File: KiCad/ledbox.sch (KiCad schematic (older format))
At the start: 0 parts

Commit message: Schematic Version 4 Some Software Changes
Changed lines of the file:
@@
 EESchema Schematic File Version 3
+LIBS:ledbox-rescue
 LIBS:power
 LIBS:device
@@
 LIBS:contrib
 LIBS:ledbox-newsymbols
+LIBS:74xxLVCxG
+LIBS:analog_devices
+LIBS:boards
+LIBS:bridge_rectifier
+LIBS:caf
+LIBS:cirrus logic
+LIBS:eeprom
+LIBS:ft232rl
+LIBS:linear_technology
+LIBS:micrel
+LIBS:NXP Semiconductor
+LIBS:SigmaDSP
+LIBS:texas_instruments
+LIBS:tl431
+LIBS:toslink
+LIBS:worldsemi
+LIBS:ac-dc
+LIBS:Altera
+LIBS:Battery_Management
+LIBS:bbd
+LIBS:Bosch
+LIBS:brooktre
+LIBS:Connector
+LIBS:dc-dc
+LIBS:Decawave
+LIBS:Diode
+LIBS:Display
+LIBS:driver_gate
+LIBS:DSP_Microchip_DSPIC33
+LIBS:elec-unifil
+LIBS:ESD_Protection
+LIBS:Espressif
+LIBS:FPGA_Actel
+LIBS:ftdi
+LIBS:gennum
+LIBS:Graphic
+LIBS:hc11
+LIBS:infineon
+LIBS:intersil
+LIBS:ir
+LIBS:Lattice
+LIBS:LED
+LIBS:LEM
+LIBS:Logic_74xgxx
+LIBS:Logic_74xx
+LIBS:Logic_CMOS_4000
+LIBS:Logic_CMOS_IEEE
+LIBS:logic_programmable
+LIBS:Logic_TTL_IEEE
+LIBS:maxim
+LIBS:MCU_Microchip_PIC10
+LIBS:MCU_Microchip_PIC12
+LIBS:MCU_Microchip_PIC16
+LIBS:MCU_Microchip_PIC18
+LIBS:MCU_Microchip_PIC24
+LIBS:MCU_Microchip_PIC32
+LIBS:MCU_NXP_Kinetis
+LIBS:MCU_NXP_LPC
+LIBS:MCU_NXP_S08
+LIBS:MCU_Parallax
+LIBS:MCU_ST_STM8
+LIBS:MCU_ST_STM32
+LIBS:MCU_Texas_MSP430
+LIBS:Mechanical
+LIBS:modules
+LIBS:motor_drivers
+LIBS:Motor
+LIBS:nordicsemi
+LIBS:nxp
+LIBS:onsemi
+LIBS:Oscillators
+LIBS:Power_Management
+LIBS:powerint
+LIBS:pspice
+LIBS:references
+LIBS:Relay
+LIBS:RF_Bluetooth
+LIBS:rfcom
+LIBS:RFSolutions
+LIBS:Sensor_Current
+LIBS:Sensor_Humidity
+LIBS:sensors
+LIBS:silabs
+LIBS:supertex
+LIBS:Switch
+LIBS:Transformer
+LIBS:Transistor
+LIBS:triac_thyristor
+LIBS:Valve
+LIBS:video
+LIBS:wiznet
+LIBS:Worldsemi
+LIBS:Xicor
+LIBS:xilinx-artix7
+LIBS:xilinx-kintex7
+LIBS:xilinx-spartan6
+LIBS:xilinx-virtex5
+LIBS:xilinx-virtex6
+LIBS:xilinx-virtex7
+LIBS:zetex
+LIBS:Zilog
 LIBS:ledbox-cache
 EELAYER 26 0
@@
 Comp "Fabian Geißler"
 Comment1 "Prototyp"
-Comment2 "Version 3"
+Comment2 "Version 4"
 Comment3 ""
 Comment4 ""
@@
 $EndSheet
 $Sheet
+S 5000 3600 1600 1700
+U 59DB9B58
+F0 "Controller" 60
+F1 "Controller.sch" 60
+F2 "TX_EN" O R 6600 4100 60
+F3 "RX" I R 6600 3900 60
+F4 "TX" O R 6600 3800 60
+F5 "BTN" I L 5000 4400 60
+F6 "LED_IR" O L 5000 4200 60
+F7 "AIN0" I R 6600 4400 60
+F8 "AIN1" I R 6600 4500 60
+F9 "LED1" O L 5000 4600 60
+F10 "LED2" O L 5000 4700 60
+F11 "PUSH1" I L 5000 4900 60
+F12 "PUSH2" I L 5000 5000 60
+F13 "~RESET" I L 5000 5100 60
+$EndSheet
+$Sheet
+S 3300 2750 1400 550
+U 59DBA013
+F0 "Supply" 60
+F1 "Supply.sch" 60
+$EndSheet
+Wire Wire Line
+	6900 3800 6600 3800
+Wire Wire Line
+	6600 3900 6900 3900
+Wire Wire Line
+	6900 4100 6600 4100
+Wire Wire Line
+	6900 4400 6600 4400
+Wire Wire Line
+	6600 4500 6900 4500
+Wire Wire Line
+	5000 4200 4700 4200
+Wire Wire Line
+	4700 4400 5000 4400
+Wire Wire Line
+	5000 4600 4700 4600
+Wire Wire Line
+	4700 4700 5000 4700
+Wire Wire Line
+	5000 4900 4700 4900
+Wire Wire Line
+	4700 5000 5000 5000
+Wire Wire Line
+	5000 5100 4700 5100
+$Sheet
 S 3300 3600 1400 1700
 U 59DBA5DF
@@
 F1 "Interface.sch" 60
 F2 "LED_IR" I R 4700 4200 60
-F3 "PWM_R" I R 4700 3800 60
-F4 "PWM_G" I R 4700 3900 60
-F5 "PWM_B" I R 4700 4000 60
-F6 "BTN" O R 4700 4400 60
-F7 "~RESET" O R 4700 5100 60
-F8 "PUSH1" O R 4700 4900 60
-F9 "PUSH2" O R 4700 5000 60
-F10 "LED1" I R 4700 4600 60
-F11 "LED2" I R 4700 4700 60
-$EndSheet
-$Sheet
-S 5000 3600 1600 1700
-U 59DB9B58
-F0 "Controller" 60
-F1 "Controller.sch" 60
-F2 "PWM_R" O L 5000 3800 60
-F3 "PWM_G" O L 5000 3900 60
-F4 "TX_EN" O R 6600 4100 60
-F5 "RX" I R 6600 3900 60
-F6 "TX" O R 6600 3800 60
-F7 "PWM_B" O L 5000 4000 60
-F8 "BTN" I L 5000 4400 60
-F9 "LED_IR" O L 5000 4200 60
-F10 "AIN0" I R 6600 4400 60
-F11 "AIN1" I R 6600 4500 60
-F12 "LED1" O L 5000 4600 60
-F13 "LED2" O L 5000 4700 60
-F14 "PUSH1" I L 5000 4900 60
-F15 "PUSH2" I L 5000 5000 60
-F16 "~RESET" I L 5000 5100 60
-$EndSheet
-$Sheet
-S 3300 2750 1400 550
-U 59DBA013
-F0 "Supply" 60
-F1 "Supply.sch" 60
-$EndSheet
-Wire Wire Line
-	6900 3800 6600 3800
-Wire Wire Line
-	6600 3900 6900 3900
-Wire Wire Line
-	6900 4100 6600 4100
-Wire Wire Line
-	6900 4400 6600 4400
-Wire Wire Line
-	6600 4500 6900 4500
-Wire Wire Line
-	5000 3800 4700 3800
-Wire Wire Line
-	4700 3900 5000 3900
-Wire Wire Line
-	5000 4000 4700 4000
-Wire Wire Line
-	5000 4200 4700 4200
-Wire Wire Line
-	4700 4400 5000 4400
-Wire Wire Line
-	5000 4600 4700 4600
-Wire Wire Line
-	4700 4700 5000 4700
-Wire Wire Line
-	5000 4900 4700 4900
-Wire Wire Line
-	4700 5000 5000 5000
-Wire Wire Line
-	5000 5100 4700 5100
+F3 "BTN" O R 4700 4400 60
+F4 "~RESET" O R 4700 5100 60
+F5 "PUSH1" O R 4700 4900 60
+F6 "PUSH2" O R 4700 5000 60
+F7 "LED1" I R 4700 4600 60
+F8 "LED2" I R 4700 4700 60
+$EndSheet
 $EndSCHEMATC

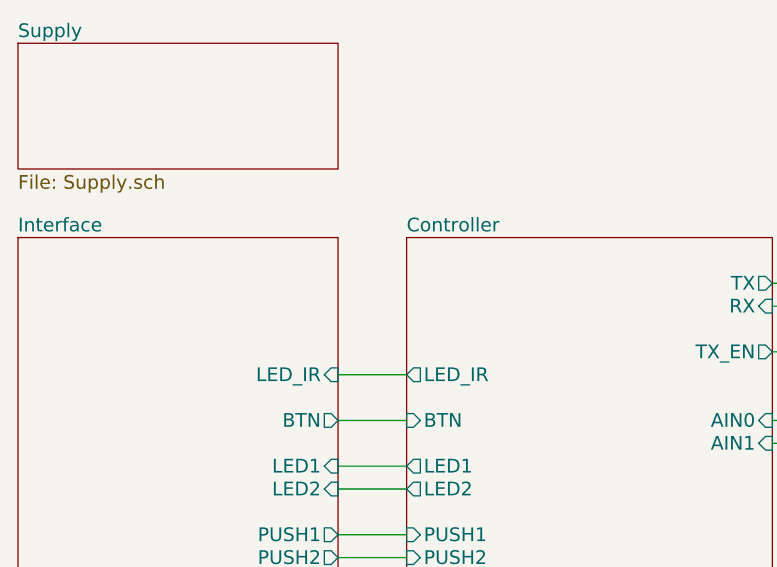
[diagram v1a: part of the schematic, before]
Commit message: Changes to V4 Schematic, new Board design
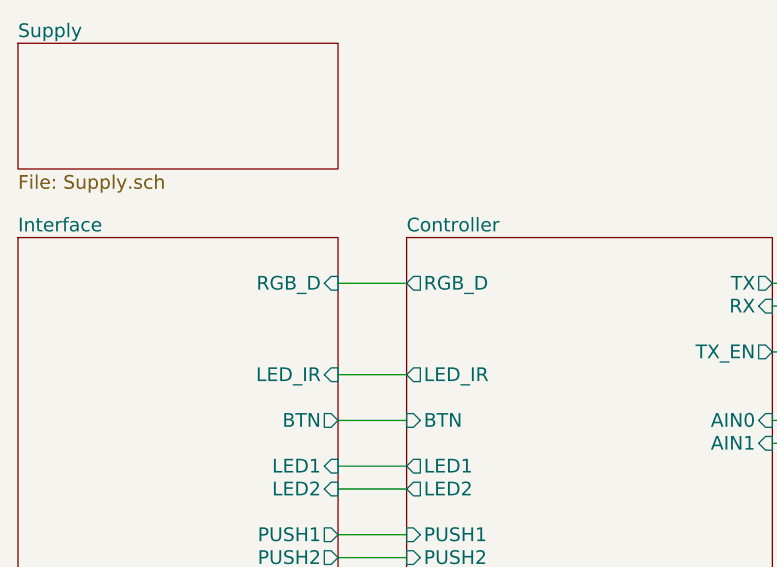
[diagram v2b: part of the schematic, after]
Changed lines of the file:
@@
 F12 "PUSH2" I L 5000 5000 60
 F13 "~RESET" I L 5000 5100 60
+F14 "RGB_D" O L 5000 3800 60
 $EndSheet
 $Sheet
@@
 F7 "LED1" I R 4700 4600 60
 F8 "LED2" I R 4700 4700 60
+F9 "RGB_D" I R 4700 3800 60
 $EndSheet
+Wire Wire Line
+	5000 3800 4700 3800
 $EndSCHEMATC

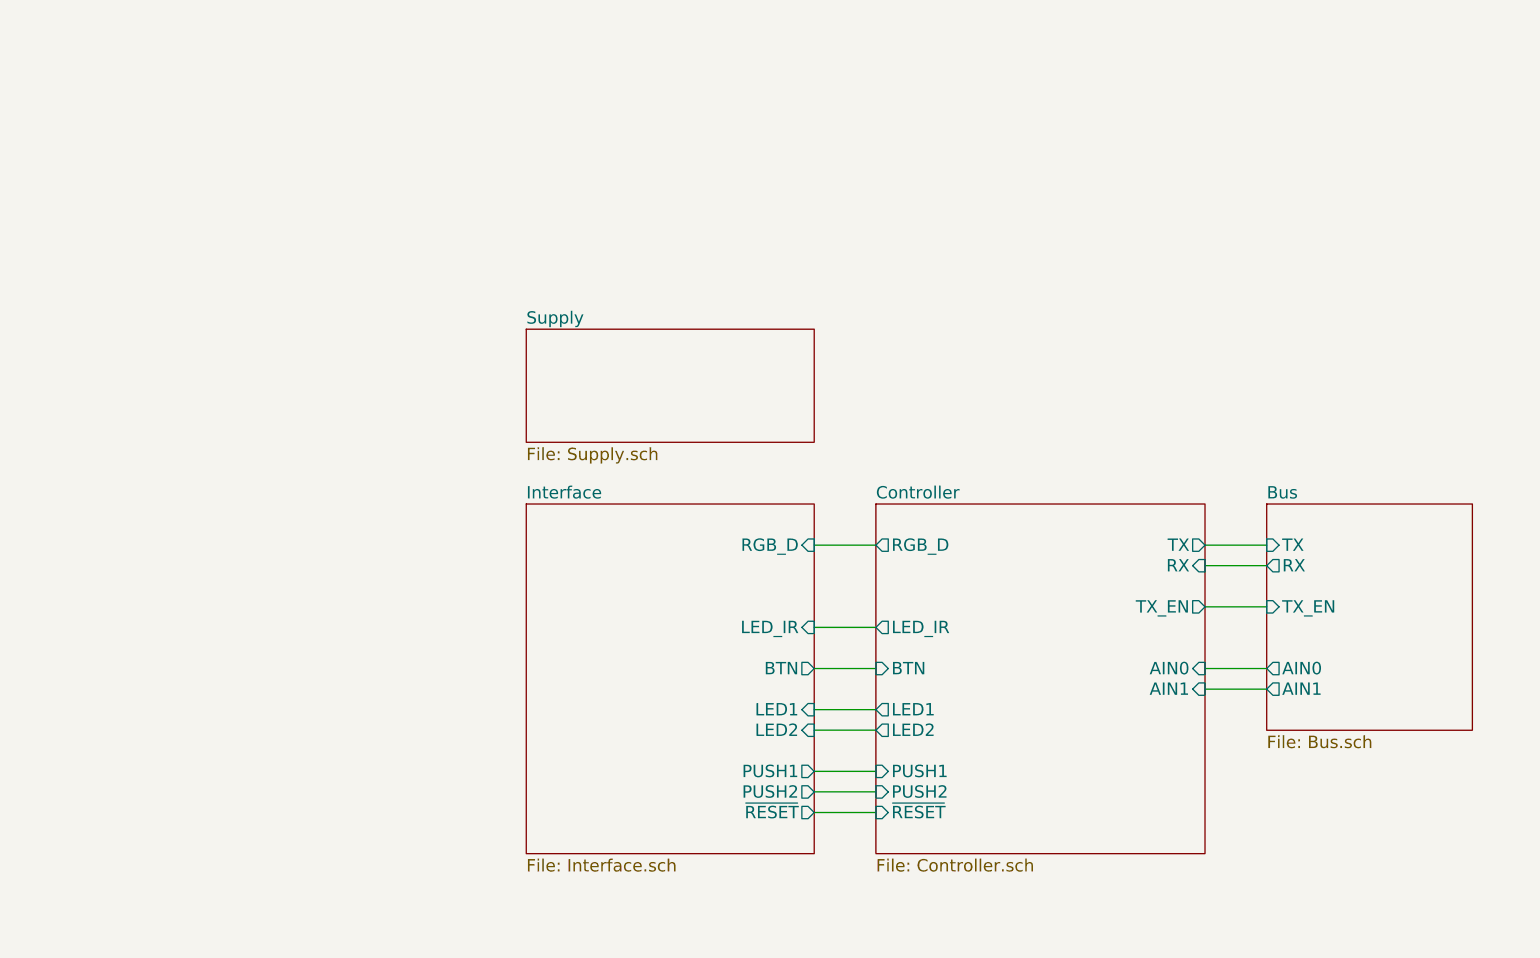
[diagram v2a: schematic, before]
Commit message: Version 4 Shift Register
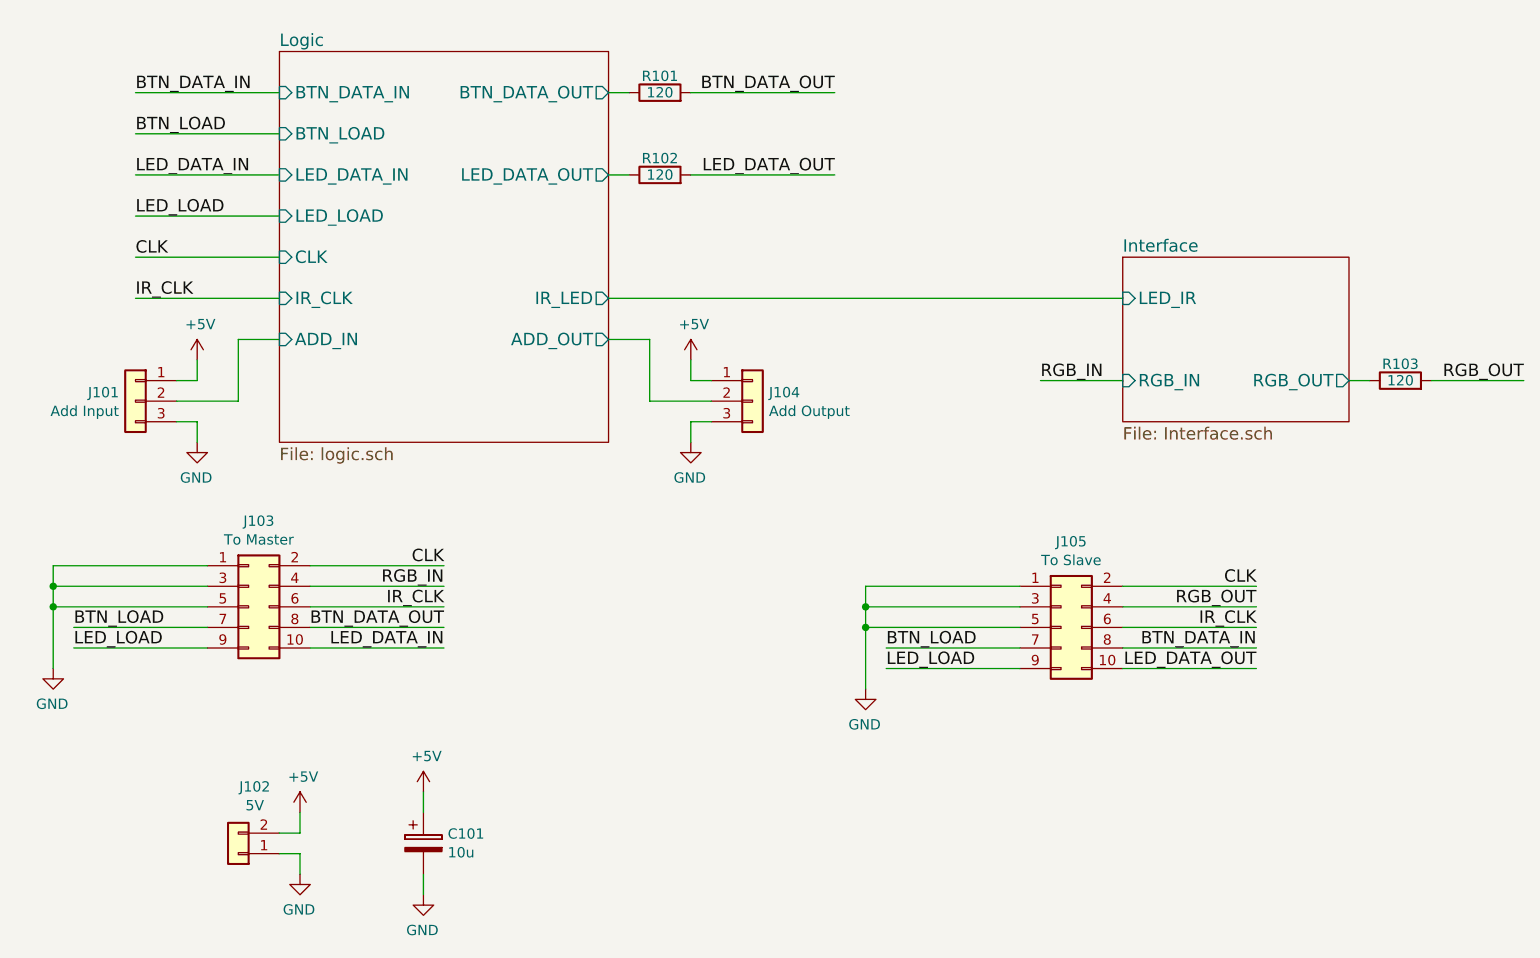
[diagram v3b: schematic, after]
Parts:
- added C101: 10u, Capacitors_THT:CP_Radial_D6.3mm_P2.50mm, symbol CP
- added J101: Add Input, Connectors_Molex:Molex_KK-6410-03_03x2.54mm_Straight, symbol Conn_01x03
- added J102: 5V, TerminalBlock_Phoenix:TerminalBlock_Phoenix_MKDS1.5-2pol, symbol Conn_01x02
- added J103: To Master, Connectors_IDC:IDC-Header_2x05_Pitch2.54mm_Straight, symbol Conn_02x05_Odd_Even
- added J104: Add Output, Connectors_Molex:Molex_KK-6410-03_03x2.54mm_Straight, symbol Conn_01x03
- added J105: To Slave, Connectors_IDC:IDC-Header_2x05_Pitch2.54mm_Straight, symbol Conn_02x05_Odd_Even
- added R101, R102, R103: 120, Resistors_SMD:R_0805, symbol R
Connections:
- new net +5V: C101.1, J101.1 (Pin_1), J102.2 (Pin_2), J104.1 (Pin_1)
- new net BTN_DATA_IN: J105.8 (Pin_8)
- new net BTN_DATA_OUT: J103.8 (Pin_8), R101.2
- new net BTN_LOAD: J103.7 (Pin_7), J105.7 (Pin_7)
- new net CLK: J103.2 (Pin_2), J105.2 (Pin_2)
- new net GND: C101.2, J101.3 (Pin_3), J102.1 (Pin_1), J103.1 (Pin_1), J103.3 (Pin_3), J103.5 (Pin_5), J104.3 (Pin_3), J105.1 (Pin_1), J105.3 (Pin_3), J105.5 (Pin_5)
- new net IR_CLK: J103.6 (Pin_6), J105.6 (Pin_6)
- new net Interface/RGB_OUT: R103.1
- new net LED_DATA_IN: J103.10 (Pin_10)
- new net LED_DATA_OUT: J105.10 (Pin_10), R102.2
- new net LED_LOAD: J103.9 (Pin_9), J105.9 (Pin_9)
- new net Logic/ADD_IN: J101.2 (Pin_2)
- new net Logic/ADD_OUT: J104.2 (Pin_2)
- new net Logic/BTN_DATA_OUT: R101.1
- new net Logic/LED_DATA_OUT: R102.1
- new net RGB_IN: J103.4 (Pin_4)
- new net RGB_OUT: J105.4 (Pin_4), R103.2

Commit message: Applied changes for final design, placed test points.
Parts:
- added TP101, TP102, TP103, TP104, TP105: Test_Point, TestPoint:TestPoint_Pad_D1.0mm, symbol ledbox-rescue:Test_Point
- C101: symbol CP -> ledbox-rescue:CP
- J101, J104: symbol Conn_01x03 -> ledbox-rescue:Conn_01x03
- J102: symbol Conn_01x02 -> ledbox-rescue:Conn_01x02
- J103, J105: symbol Conn_02x05_Odd_Even -> ledbox-rescue:Conn_02x05_Odd_Even
- R101, R102, R103: symbol R -> ledbox-rescue:R
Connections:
- net BTN_DATA_IN: now also TP103.1
- net BTN_DATA_OUT: now also TP104.1
- net CLK: now also TP101.1
- net LED_DATA_OUT: now also TP105.1
- net LED_LOAD: now also TP102.1

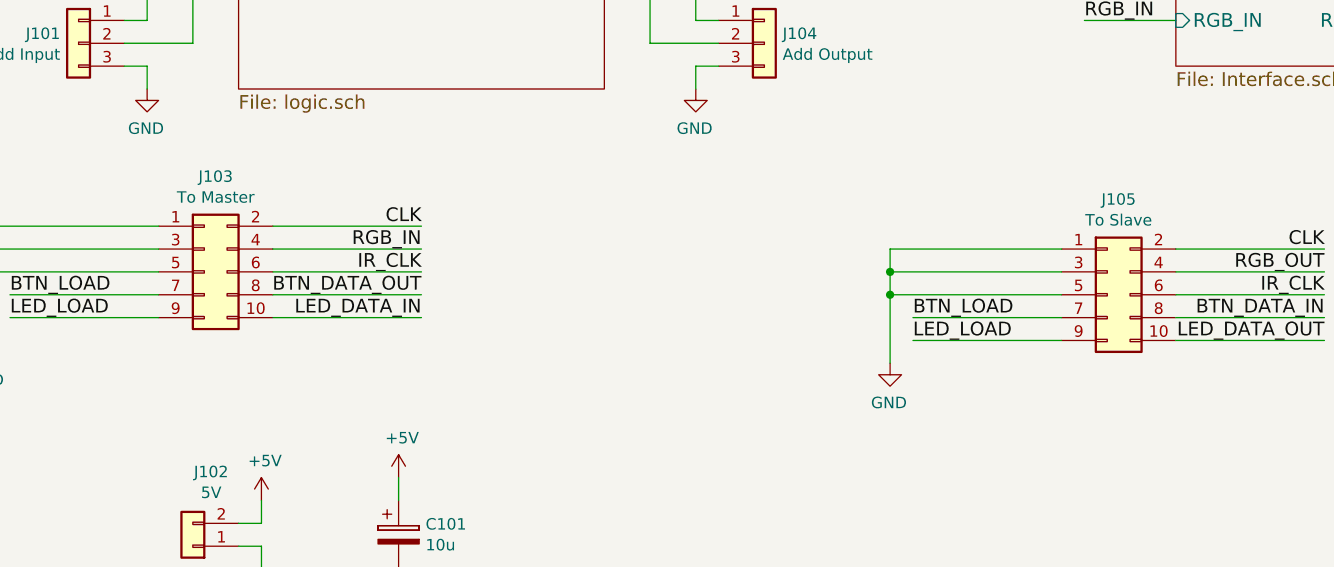
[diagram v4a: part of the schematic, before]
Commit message: turned data connectors to match cable layout
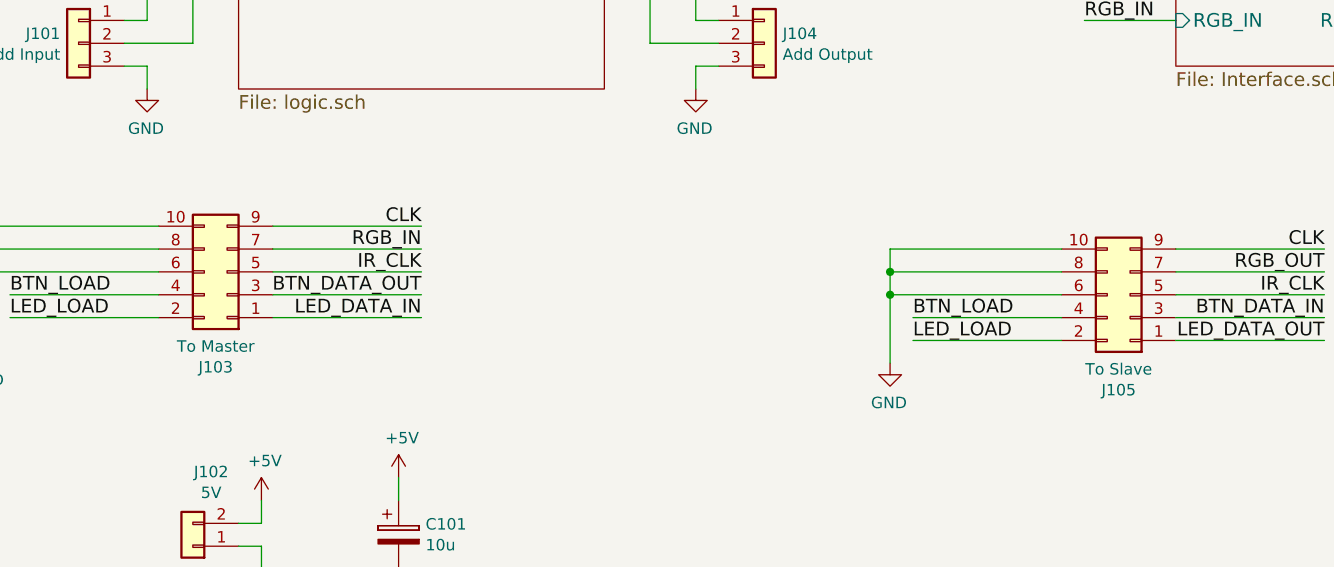
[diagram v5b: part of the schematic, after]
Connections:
- net BTN_DATA_IN: now also J105.3 (Pin_3); no longer J105.8 (Pin_8)
- net BTN_DATA_OUT: now also J103.3 (Pin_3); no longer J103.8 (Pin_8)
- net BTN_LOAD: now also J103.4 (Pin_4), J105.4 (Pin_4); no longer J103.7 (Pin_7), J105.7 (Pin_7)
- net CLK: now also J103.9 (Pin_9), J105.9 (Pin_9); no longer J103.2 (Pin_2), J105.2 (Pin_2)
- net GND: now also J103.10 (Pin_10), J103.6 (Pin_6), J103.8 (Pin_8), J105.10 (Pin_10), J105.6 (Pin_6), J105.8 (Pin_8); no longer J103.1 (Pin_1), J103.3 (Pin_3), J103.5 (Pin_5), J105.1 (Pin_1), J105.3 (Pin_3), J105.5 (Pin_5)
- net IR_CLK: now also J103.5 (Pin_5), J105.5 (Pin_5); no longer J103.6 (Pin_6), J105.6 (Pin_6)
- net LED_DATA_IN: now also J103.1 (Pin_1); no longer J103.10 (Pin_10)
- net LED_DATA_OUT: now also J105.1 (Pin_1); no longer J105.10 (Pin_10)
- net LED_LOAD: now also J103.2 (Pin_2), J105.2 (Pin_2); no longer J103.9 (Pin_9), J105.9 (Pin_9)
- net RGB_IN: now also J103.7 (Pin_7); no longer J103.4 (Pin_4)
- net RGB_OUT: now also J105.7 (Pin_7); no longer J105.4 (Pin_4)
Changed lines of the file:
@@
 L ledbox-rescue:Conn_02x05_Odd_Even J103
 U 1 1 5AE133E6
-P 1950 4100
-F 0 "J103" H 2000 4517 50  0000 C CNN
-F 1 "To Master" H 2000 4426 50  0000 C CNN
-F 2 "Connectors_IDC:IDC-Header_2x05_Pitch2.54mm_Straight" H 1950 4100 50  0001 C CNN
-F 3 "~" H 1950 4100 50  0001 C CNN
-	1    1950 4100
-	1    0    0    -1
+P 2050 4100
+F 0 "J103" H 2100 4517 50  0000 C CNN
+F 1 "To Master" H 2100 4426 50  0000 C CNN
+F 2 "Connectors_IDC:IDC-Header_2x05_Pitch2.54mm_Straight" H 2050 4100 50  0001 C CNN
+F 3 "~" H 2050 4100 50  0001 C CNN
+	1    2050 4100
+	-1   0    0    1
 $EndComp
 Wire Wire Line
@@
 L ledbox-rescue:Conn_02x05_Odd_Even J105
 U 1 1 5AE178D2
-P 5900 4200
-F 0 "J105" H 5950 4617 50  0000 C CNN
-F 1 "To Slave" H 5950 4526 50  0000 C CNN
-F 2 "Connectors_IDC:IDC-Header_2x05_Pitch2.54mm_Straight" H 5900 4200 50  0001 C CNN
-F 3 "~" H 5900 4200 50  0001 C CNN
-	1    5900 4200
-	1    0    0    -1
+P 6000 4200
+F 0 "J105" H 6050 4617 50  0000 C CNN
+F 1 "To Slave" H 6050 4526 50  0000 C CNN
+F 2 "Connectors_IDC:IDC-Header_2x05_Pitch2.54mm_Straight" H 6000 4200 50  0001 C CNN
+F 3 "~" H 6000 4200 50  0001 C CNN
+	1    6000 4200
+	-1   0    0    1
 $EndComp
 Wire Wire Line
